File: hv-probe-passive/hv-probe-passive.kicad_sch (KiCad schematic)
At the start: 20 parts, among them J2 OUT

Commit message: cleaned up the schematic and readme
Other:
- moved on the sheet: C1, C10, C11, C12, C2, C3, C4, C5, C6, C7, C8, C9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

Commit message: testing further readme improvements
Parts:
- C6, C7: MPN Nr prod.: VJ1206A222FFBAT -> VJ1206A222FFBAT
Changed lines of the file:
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@@
 			)
 		)
-		(property "MPN" "Nr prod.: VJ1206A222FFBAT"
+		(property "MPN" "VJ1206A222FFBAT"
 			(at 38.1 55.88 0)
 			(hide yes)
@@
 			)
 		)
-		(property "MPN" "Nr prod.: VJ1206A222FFBAT"
+		(property "MPN" "VJ1206A222FFBAT"
 			(at 45.72 55.88 0)
 			(hide yes)

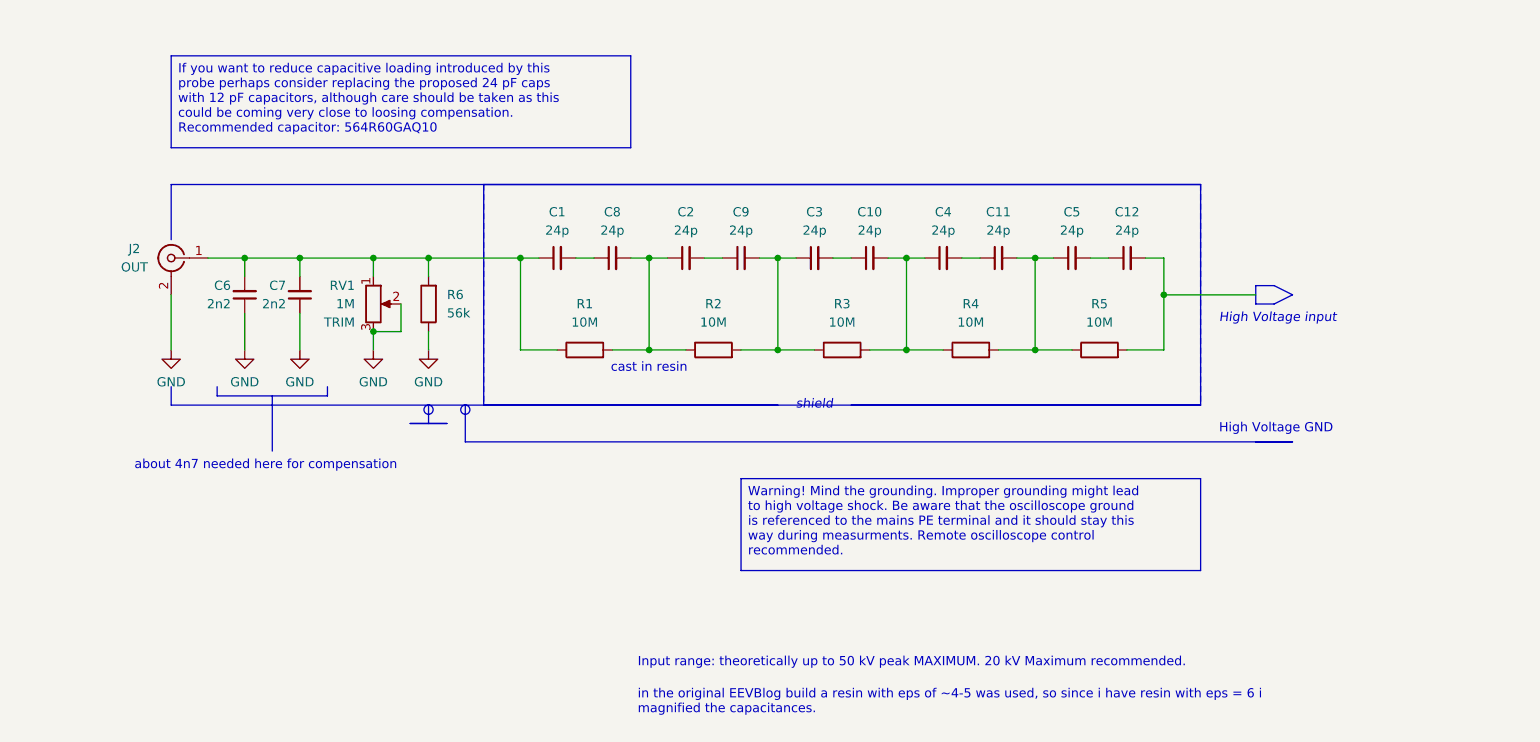
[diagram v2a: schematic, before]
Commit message: readme improvements, schematic notes update
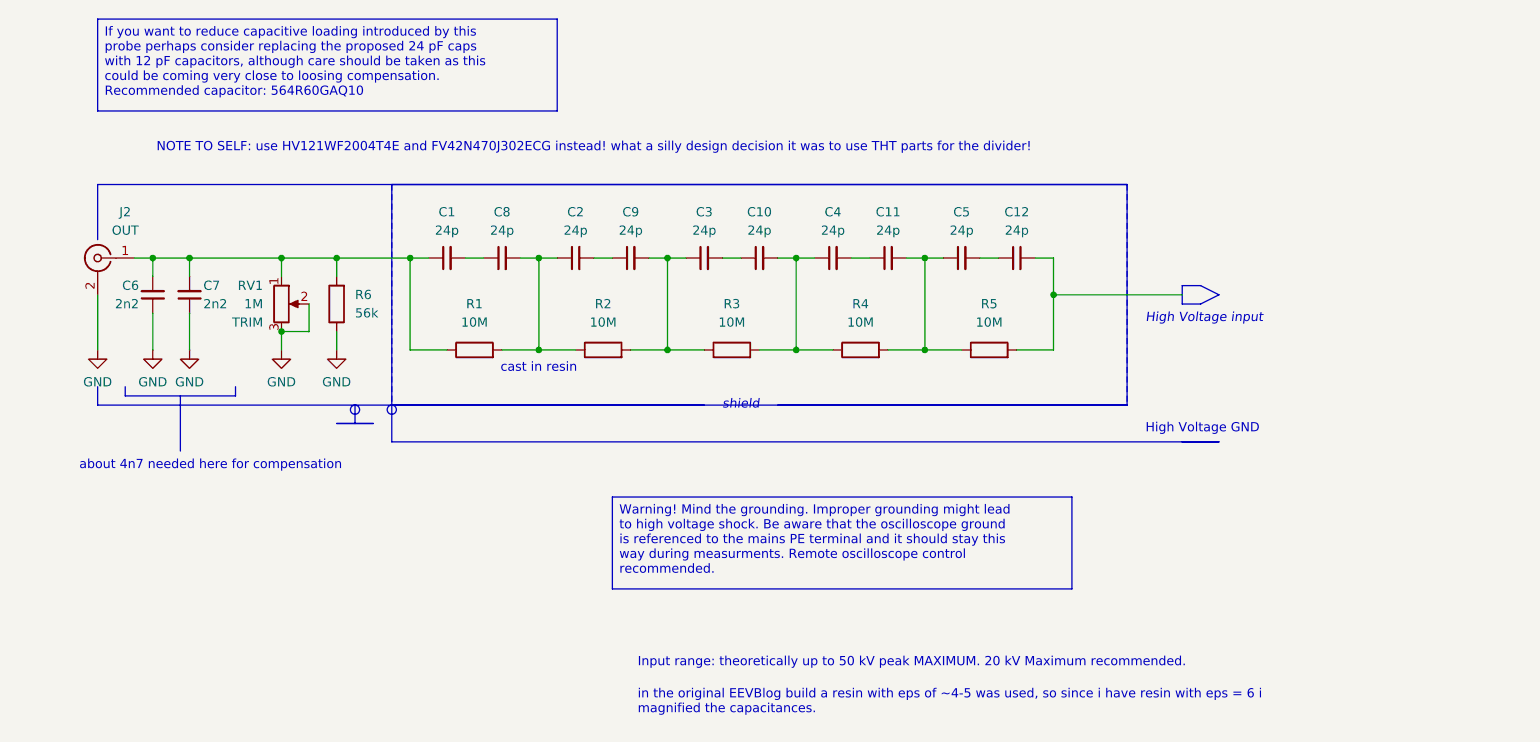
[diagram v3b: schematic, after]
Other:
- note added: "NOTE TO SELF: use HV121WF2004T4E and FV42N470J302ECG instead! what a silly design decision it was to use THT parts for the divider!"
- moved on the sheet: C1, C10, C11, C12, C2, C3, C4, C5, C6, C7, C8, C9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
